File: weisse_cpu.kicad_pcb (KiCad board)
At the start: 2 copper layers, 310 x 260 mm, 22 parts

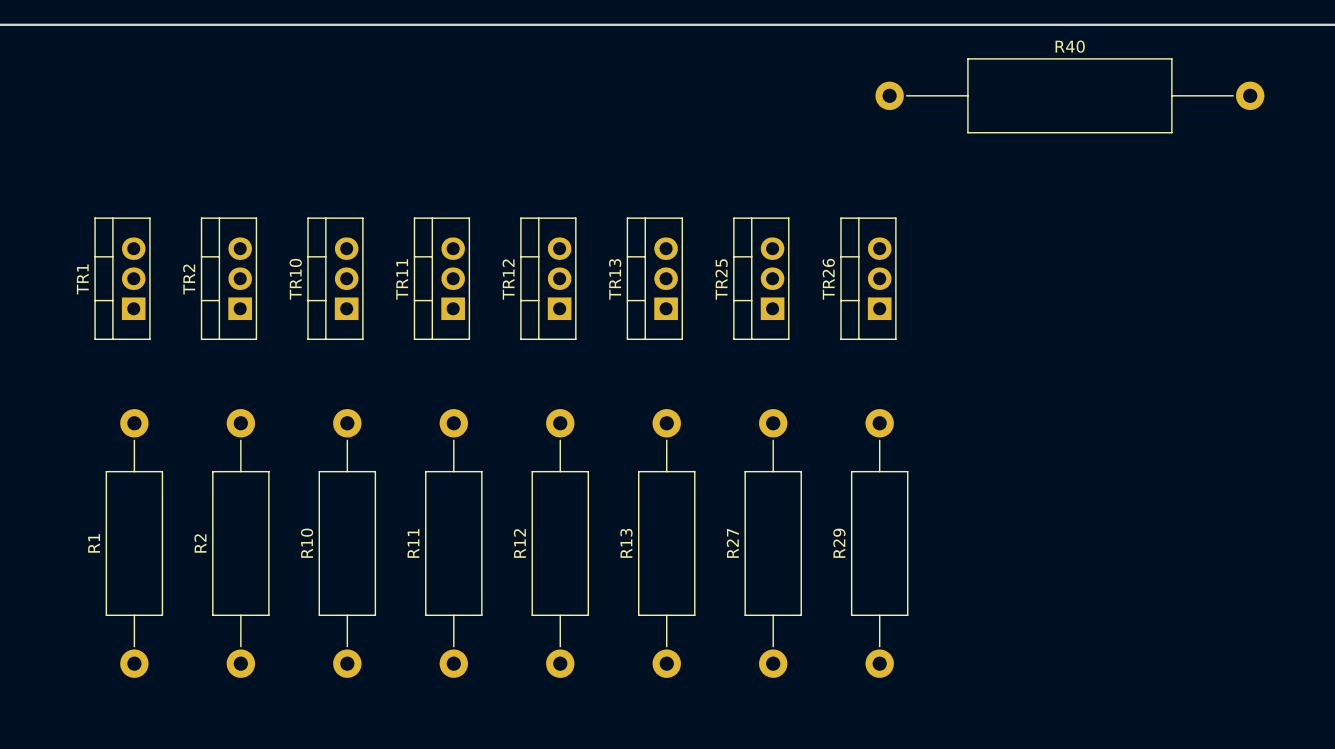
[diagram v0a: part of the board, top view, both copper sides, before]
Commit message: add a bunch of traces
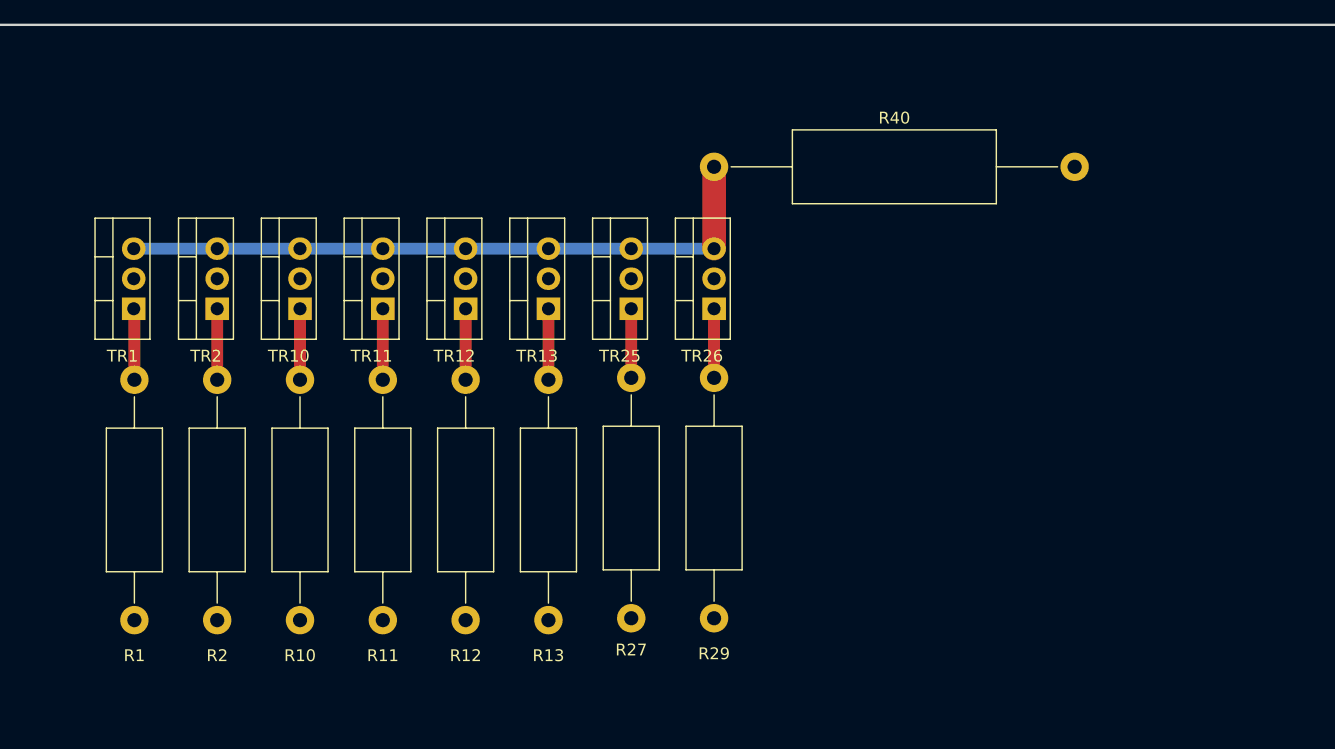
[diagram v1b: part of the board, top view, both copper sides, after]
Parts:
- moved R40 16.0 mm to (216.0, 92.0)
- moved R29 14.5 mm to (216.0, 130.2)
- moved TR26 14.0 mm to (216.0, 104.0)
- moved R27 12.6 mm to (209.0, 130.2)
- moved TR25 11.9 mm to (209.0, 104.0)
- moved R13 10.7 mm to (202.0, 130.3)
- moved TR13 9.94 mm to (202.0, 104.0)
- moved R12 8.81 mm to (195.0, 130.3)
- moved TR12 7.94 mm to (195.0, 104.0)
- moved R11 7.04 mm to (188.0, 130.3)
- moved TR11 5.94 mm to (188.0, 104.0)
- moved R10 5.44 mm to (181.0, 130.3)
- moved R2 4.19 mm to (174.0, 130.3)
- moved TR10 3.94 mm to (181.0, 104.0)
- moved R1 3.68 mm to (167.0, 130.3)
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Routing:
- net Net-(R40-Pad1): track 0.00 -> 56.0 mm
- net Net-(R1-Pad2): track 0.00 -> 6.02 mm
- net Net-(R2-Pad2): track 0.00 -> 6.00 mm
- net Net-(R13-Pad2): track 0.00 -> 6.00 mm
- net Net-(R12-Pad2): track 0.00 -> 6.00 mm
- net Net-(R11-Pad2): track 0.00 -> 6.00 mm
- net Net-(R10-Pad2): track 0.00 -> 6.00 mm
- net Net-(R29-Pad2): track 0.00 -> 5.84 mm
- net Net-(R27-Pad2): track 0.00 -> 5.84 mm

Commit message: serviceabzeige
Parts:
- added ICG10-1: 4066, Package_DIP:DIP-14_W7.62mm, F.Cu at (377.4, 224.8)
- added ICK11: LM324, Package_DIP:DIP-14_W7.62mm, F.Cu at (377.9, 207.6)
- added RM81: R_Pack08, Package_DIP:DIP-16_W7.62mm, F.Cu at (405.1, 224.8)
- added SERVICEANZEIGE+TASTATUR1: Conn_01x20_Male, Connector_PinHeader_2.00mm:PinHeader_1x20_P2.00mm_Vertical, F.Cu at (442.0, 193.0)
- added SIGNALNETZ1: Conn_01x06_Male, Connector_PinHeader_2.00mm:PinHeader_1x06_P2.00mm_Vertical, F.Cu at (442.0, 286.0)
- TR13: value BDX34B -> BDX54C
- moved EINGAENGE1 223.0 mm to (189.0, 88.0)
- moved LEISTUNGSNETZ1 3.61 mm to (442.0, 97.0)
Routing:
- net Net-(LAMPENSPALTEN1-Pad7): track 0.00 -> 2.00 mm
- net Net-(LAMPENSPALTEN1-Pad5): track 0.00 -> 2.00 mm
- net Net-(LAMPENSPALTEN1-Pad3): track 0.00 -> 2.00 mm
- net Net-(LAMPENSPALTEN1-Pad15): track 0.00 -> 2.00 mm
- net Net-(LAMPENSPALTEN1-Pad13): track 0.00 -> 2.00 mm
- net Net-(LAMPENSPALTEN1-Pad11): track 0.00 -> 2.00 mm
- net Net-(LAMPENSPALTEN1-Pad10): track 0.00 -> 2.00 mm
- net Net-(LAMPENSPALTEN1-Pad1): track 0.00 -> 2.00 mm

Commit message: move transistors down
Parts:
- moved R1 11.8 mm to (167.0, 142.2)
- moved R10 11.8 mm to (181.0, 142.2)
- moved R11 11.8 mm to (188.0, 142.2)
- moved R12 11.8 mm to (195.0, 142.2)
- moved R13 11.8 mm to (202.0, 142.2)
- moved R2 11.8 mm to (174.0, 142.2)
- moved R27 11.8 mm to (209.0, 142.0)
- moved R29 11.8 mm to (216.0, 142.0)
- moved TR1 11.8 mm to (166.9, 115.8)
- moved TR10 11.8 mm to (181.0, 115.8)
- moved TR11 11.8 mm to (188.0, 115.8)
- moved TR12 11.8 mm to (195.0, 115.8)
- moved TR13 11.8 mm to (202.0, 115.8)
- moved TR2 11.8 mm to (174.0, 115.8)
- moved TR25 11.8 mm to (209.0, 115.8)
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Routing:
- added copper zone on F.Cu, net GND
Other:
- outline, holes or cut-outs redrawn

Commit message: move connectors
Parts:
- moved ICH4-1 22.1 mm to (238.3, 188.6)
- moved ICG10-1 18.0 mm to (376.5, 206.8)
- moved ICK11 18.0 mm to (377.0, 189.6)
- moved RM81 18.0 mm to (404.2, 206.8)
- moved SERVICEANZEIGE+TASTATUR1 15.0 mm to (442.0, 178.0)
- moved R40 9.03 mm to (222.8, 98.0)
- moved EINGAENGE1 4.00 mm to (193.0, 88.0)
- moved R1 2.24 mm to (169.0, 143.2)
- moved R10 2.24 mm to (183.0, 143.2)
- moved R11 2.24 mm to (190.0, 143.2)
- moved R12 2.24 mm to (197.0, 143.2)
- moved R13 2.24 mm to (204.0, 143.2)
- moved R2 2.24 mm to (176.0, 143.2)
- moved R27 2.24 mm to (211.0, 143.0)
- moved R29 2.24 mm to (218.0, 143.0)
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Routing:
- net Net-(R40-Pad1): track 56.0 -> 49.1 mm
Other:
- outline, holes or cut-outs redrawn

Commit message: move holes
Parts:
- moved R40 5.00 mm to (222.8, 103.0)
- moved LAMPENSPALTEN1 3.16 mm to (148.0, 120.0)
- moved TR32 2.00 mm to (222.0, 162.5)
- moved R1 1.00 mm to (170.0, 143.2)
- moved R10 1.00 mm to (184.0, 143.2)
- moved R11 1.00 mm to (191.0, 143.2)
- moved R12 1.00 mm to (198.0, 143.2)
- moved R13 1.00 mm to (205.0, 143.2)
- moved R2 1.00 mm to (177.0, 143.2)
- moved R27 1.00 mm to (212.0, 143.0)
- moved R29 1.00 mm to (219.0, 143.0)
- moved TR1 1.00 mm to (169.9, 116.8)
- moved TR10 1.00 mm to (184.0, 116.8)
- moved TR11 1.00 mm to (191.0, 116.8)
- moved TR12 1.00 mm to (198.0, 116.8)
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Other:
- outline, holes or cut-outs redrawn

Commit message: add eeprom
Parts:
- added ICC6: 628128_DIP32_SSOP32, Package_DIP:DIP-24_W15.24mm, F.Cu at (300.1, 271.0)
- added ICD6: 27128, Package_DIP:DIP-28_W15.24mm, F.Cu at (295.0, 251.0)
- added ICE6: 27128, Package_DIP:DIP-28_W15.24mm, F.Cu at (295.0, 232.6)
- moved ICG10-1 6.71 mm to (382.5, 203.8)
- moved ICK11 6.71 mm to (383.0, 186.6)
- moved RM81 6.71 mm to (410.2, 203.8)
- moved ICH4-1 3.82 mm to (241.8, 187.0)
- moved R11 3.01 mm to (194.0, 143.4)
- moved R12 3.01 mm to (201.0, 143.4)
- moved R13 3.01 mm to (208.0, 143.4)
- moved R27 3.01 mm to (215.0, 143.2)
- moved R29 3.01 mm to (222.0, 143.2)
- moved TR11 3.01 mm to (194.0, 117.1)
- moved TR12 3.01 mm to (201.0, 117.1)
- moved TR13 3.01 mm to (208.0, 117.1)
- moved TR25 3.01 mm to (215.0, 117.1)
- moved TR26 3.01 mm to (222.0, 117.1)
- moved R10 2.01 mm to (186.0, 143.4)
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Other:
- outline, holes or cut-outs redrawn

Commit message: new photo and new holes
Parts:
- moved ICC6 17.2 mm to (302.6, 288.0)
- moved ICD6 17.2 mm to (297.5, 268.0)
- moved ICE6 17.2 mm to (297.5, 249.6)
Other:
- outline, holes or cut-outs redrawn
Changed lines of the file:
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@@
   )
   (footprint "Package_DIP:DIP-24_W15.24mm" (layer "F.Cu")
-    (at 300.06 271 90)
+    (at 302.56 288 90)
     (descr "24-lead though-hole mounted DIP package, row spacing 15.24 mm (600 mils)")
     (tags "THT DIP DIL PDIP 2.54mm 15.24mm 600mil")
@@
   )
   (footprint "Package_DIP:DIP-28_W15.24mm" (layer "F.Cu")
-    (at 295.015 251.015 90)
+    (at 297.515 268.015 90)
     (descr "28-lead though-hole mounted DIP package, row spacing 15.24 mm (600 mils)")
     (tags "THT DIP DIL PDIP 2.54mm 15.24mm 600mil")
@@
   )
   (footprint "Package_DIP:DIP-28_W15.24mm" (layer "F.Cu")
-    (at 295.015 232.615 90)
+    (at 297.515 249.615 90)
     (descr "28-lead though-hole mounted DIP package, row spacing 15.24 mm (600 mils)")
     (tags "THT DIP DIL PDIP 2.54mm 15.24mm 600mil")
@@
     )
   )
+  (gr_circle (center 350.5 335) (end 353 335)
+    (stroke (width 0.1) (type default)) (fill none) (layer "Edge.Cuts"))
   (gr_line (start 450 340) (end 140 340)
     (stroke (width 0.2) (type solid)) (layer "Edge.Cuts"))
   (gr_line (start 450 80) (end 450 340)
     (stroke (width 0.2) (type solid)) (layer "Edge.Cuts"))
-  (gr_circle (center 232 85) (end 234 85)
+  (gr_circle (center 232 85) (end 234.5 85)
     (stroke (width 0.1) (type default)) (fill none) (layer "Edge.Cuts"))
-  (gr_circle (center 382 85) (end 384 85)
+  (gr_circle (center 381 85) (end 383.5 85)
+    (stroke (width 0.1) (type default)) (fill none) (layer "Edge.Cuts"))
+  (gr_circle (center 201.5 335) (end 204 335)
     (stroke (width 0.1) (type default)) (fill none) (layer "Edge.Cuts"))
   (gr_line (start 140 340) (end 140 80)
     (stroke (width 0.2) (type solid)) (layer "Edge.Cuts"))
+  (gr_circle (center 300 335) (end 301.5 335)
+    (stroke (width 0.1) (type default)) (fill none) (layer "Edge.Cuts"))
   (gr_line (start 140 80) (end 450 80)
     (stroke (width 0.2) (type solid)) (layer "Edge.Cuts"))
-  (gr_circle (center 301 85) (end 302 85)
+  (gr_circle (center 296 85) (end 297.5 85)
     (stroke (width 0.1) (type default)) (fill none) (layer "Edge.Cuts"))
-  (gr_circle (center 281 85) (end 282 85)
+  (gr_circle (center 291 335) (end 292.5 335)
     (stroke (width 0.1) (type default)) (fill none) (layer "Edge.Cuts"))
+  (gr_circle (center 287 85) (end 288.5 85)
+    (stroke (width 0.1) (type default)) (fill none) (layer "Edge.Cuts"))
+  (dimension (type aligned) (layer "Edge.Cuts")
+    (pts (xy 201.5 335) (xy 350.5 335))
+    (height 20.5)
+    (gr_text "149,0000 mm" (at 276 354.35) (layer "Edge.Cuts")
+      (effects (font (size 1 1) (thickness 0.15)))
+    )
+    (format (prefix "") (suffix "") (units 3) (units_format 1) (precision 4))
+    (style (thickness 0.1) (arrow_length 1.27) (text_position_mode 0) (extension_height 0.58642) (extension_offset 0.5) keep_text_aligned)
+  )
+  (dimension (type aligned) (layer "Edge.Cuts")
+    (pts (xy 287 85) (xy 296 85))
+    (height -10)
+    (gr_text "9,0000 mm" (at 291.5 73.85) (layer "Edge.Cuts")
+      (effects (font (size 1 1) (thickness 0.15)))
+    )
+    (format (prefix "") (suffix "") (units 3) (units_format 1) (precision 4))
+    (style (thickness 0.1) (arrow_length 1.27) (text_position_mode 0) (extension_height 0.58642) (extension_offset 0.5) keep_text_aligned)
+  )
+  (dimension (type aligned) (layer "Edge.Cuts")
+    (pts (xy 232 85) (xy 381 85))
+    (height -21)
+    (gr_text "149,0000 mm" (at 306.5 62.85) (layer "Edge.Cuts")
+      (effects (font (size 1 1) (thickness 0.15)))
+    )
+    (format (prefix "") (suffix "") (units 3) (units_format 1) (precision 4))
+    (style (thickness 0.1) (arrow_length 1.27) (text_position_mode 0) (extension_height 0.58642) (extension_offset 0.5) keep_text_aligned)
+  )
+  (dimension (type aligned) (layer "Edge.Cuts")
+    (pts (xy 291 335) (xy 300 335))
+    (height 15)
+    (gr_text "9,0000 mm" (at 295.5 348.85) (layer "Edge.Cuts")
+      (effects (font (size 1 1) (thickness 0.15)))
+    )
+    (format (prefix "") (suffix "") (units 3) (units_format 1) (precision 4))
+    (style (thickness 0.1) (arrow_length 1.27) (text_position_mode 0) (extension_height 0.58642) (extension_offset 0.5) keep_text_aligned)
+  )
+  (dimension (type aligned) (layer "Edge.Cuts")
+    (pts (xy 232 85) (xy 287 85))
+    (height -8)
+    (gr_text "55,0000 mm" (at 259.5 75.85) (layer "Edge.Cuts")
+      (effects (font (size 1 1) (thickness 0.15)))
+    )
+    (format (prefix "") (suffix "") (units 3) (units_format 1) (precision 4))
+    (style (thickness 0.1) (arrow_length 1.27) (text_position_mode 0) (extension_height 0.58642) (extension_offset 0.5) keep_text_aligned)
+  )
+  (dimension (type aligned) (layer "Edge.Cuts")
+    (pts (xy 296 85) (xy 381 85))
+    (height -7)
+    (gr_text "85,0000 mm" (at 338.5 76.85) (layer "Edge.Cuts")
+      (effects (font (size 1 1) (thickness 0.15)))
+    )
+    (format (prefix "") (suffix "") (units 3) (units_format 1) (precision 4))
+    (style (thickness 0.1) (arrow_length 1.27) (text_position_mode 0) (extension_height 0.58642) (extension_offset 0.5) keep_text_aligned)
+  )
   (segment (start 148 118) (end 148 120) (width 1) (layer "F.Cu") (net 135))
   (segment (start 148 114) (end 148 116) (width 1) (layer "F.Cu") (net 136))

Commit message: mirror board
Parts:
- moved ICE6 7.15 mm to (303.0, 245.0)
- moved ICD6 6.02 mm to (303.0, 265.5)
- moved ICC6 5.70 mm to (308.1, 286.5)
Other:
- outline, holes or cut-outs redrawn
- board text added: "ICC6"
- board text added: "ICD6"
- board text added: "ICE6"
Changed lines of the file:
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@@
   )
   (footprint "Package_DIP:DIP-24_W15.24mm" (layer "F.Cu")
-    (at 302.56 288 90)
+    (at 308.06 286.5 90)
     (descr "24-lead though-hole mounted DIP package, row spacing 15.24 mm (600 mils)")
     (tags "THT DIP DIL PDIP 2.54mm 15.24mm 600mil")
@@
   )
   (footprint "Package_DIP:DIP-28_W15.24mm" (layer "F.Cu")
-    (at 297.515 268.015 90)
+    (at 302.98 265.5 90)
     (descr "28-lead though-hole mounted DIP package, row spacing 15.24 mm (600 mils)")
     (tags "THT DIP DIL PDIP 2.54mm 15.24mm 600mil")
@@
   )
   (footprint "Package_DIP:DIP-28_W15.24mm" (layer "F.Cu")
-    (at 297.515 249.615 90)
+    (at 302.98 245 90)
     (descr "28-lead though-hole mounted DIP package, row spacing 15.24 mm (600 mils)")
     (tags "THT DIP DIL PDIP 2.54mm 15.24mm 600mil")
@@
     )
   )
-  (gr_circle (center 350.5 335) (end 353 335)
+  (gr_rect (start 306.5 270) (end 337.5 287.5)
+    (stroke (width 0.15) (type default)) (fill none) (layer "B.SilkS"))
+  (gr_rect (start 301.5 228.5) (end 337.5 246)
+    (stroke (width 0.15) (type default)) (fill none) (layer "B.SilkS"))
+  (gr_rect (start 301.5 249) (end 337.5 266.5)
+    (stroke (width 0.15) (type default)) (fill none) (layer "B.SilkS"))
+  (gr_circle (center 354 335) (end 356.5 335)
     (stroke (width 0.1) (type default)) (fill none) (layer "Edge.Cuts"))
   (gr_line (start 450 340) (end 140 340)
@@
   (gr_line (start 450 80) (end 450 340)
     (stroke (width 0.2) (type solid)) (layer "Edge.Cuts"))
-  (gr_circle (center 232 85) (end 234.5 85)
+  (gr_circle (center 234 85) (end 236.5 85)
     (stroke (width 0.1) (type default)) (fill none) (layer "Edge.Cuts"))
-  (gr_circle (center 381 85) (end 383.5 85)
+  (gr_circle (center 383 85) (end 385.5 85)
     (stroke (width 0.1) (type default)) (fill none) (layer "Edge.Cuts"))
-  (gr_circle (center 201.5 335) (end 204 335)
+  (gr_circle (center 205 335) (end 207.5 335)
     (stroke (width 0.1) (type default)) (fill none) (layer "Edge.Cuts"))
   (gr_line (start 140 340) (end 140 80)
     (stroke (width 0.2) (type solid)) (layer "Edge.Cuts"))
-  (gr_circle (center 300 335) (end 301.5 335)
+  (gr_circle (center 303.5 335) (end 305 335)
     (stroke (width 0.1) (type default)) (fill none) (layer "Edge.Cuts"))
   (gr_line (start 140 80) (end 450 80)
     (stroke (width 0.2) (type solid)) (layer "Edge.Cuts"))
-  (gr_circle (center 296 85) (end 297.5 85)
+  (gr_circle (center 298 85) (end 299.5 85)
     (stroke (width 0.1) (type default)) (fill none) (layer "Edge.Cuts"))
-  (gr_circle (center 291 335) (end 292.5 335)
+  (gr_circle (center 294.5 335) (end 296 335)
     (stroke (width 0.1) (type default)) (fill none) (layer "Edge.Cuts"))
-  (gr_circle (center 287 85) (end 288.5 85)
+  (gr_circle (center 289 85) (end 290.5 85)
     (stroke (width 0.1) (type default)) (fill none) (layer "Edge.Cuts"))
-  (dimension (type aligned) (layer "Edge.Cuts")
-    (pts (xy 201.5 335) (xy 350.5 335))
+  (gr_text "ICD6" (at 312 257.5) (layer "B.SilkS")
+    (effects (font (size 1 1) (thickness 0.15)) (justify mirror))
+  )
+  (gr_text "ICE6" (at 311.5 236) (layer "B.SilkS")
+    (effects (font (size 1 1) (thickness 0.15)) (justify mirror))
+  )
+  (gr_text "ICC6" (at 317 275.5) (layer "B.SilkS")
+    (effects (font (size 1 1) (thickness 0.15)) (justify mirror))
+  )
+  (dimension (type aligned) (layer "User.1")
+    (pts (xy 205 335) (xy 354 335))
     (height 20.5)
-    (gr_text "149,0000 mm" (at 276 354.35) (layer "Edge.Cuts")
+    (gr_text "149,0000 mm" (at 279.5 354.35) (layer "User.1")
       (effects (font (size 1 1) (thickness 0.15)))
     )
@@
     (style (thickness 0.1) (arrow_length 1.27) (text_position_mode 0) (extension_height 0.58642) (extension_offset 0.5) keep_text_aligned)
   )
-  (dimension (type aligned) (layer "Edge.Cuts")
-    (pts (xy 287 85) (xy 296 85))
+  (dimension (type aligned) (layer "User.1")
+    (pts (xy 289 85) (xy 298 85))
     (height -10)
-    (gr_text "9,0000 mm" (at 291.5 73.85) (layer "Edge.Cuts")
+    (gr_text "9,0000 mm" (at 293.5 73.85) (layer "User.1")
       (effects (font (size 1 1) (thickness 0.15)))
     )
@@
     (style (thickness 0.1) (arrow_length 1.27) (text_position_mode 0) (extension_height 0.58642) (extension_offset 0.5) keep_text_aligned)
   )
-  (dimension (type aligned) (layer "Edge.Cuts")
-    (pts (xy 232 85) (xy 381 85))
+  (dimension (type aligned) (layer "User.1")
+    (pts (xy 234 85) (xy 383 85))
     (height -21)
-    (gr_text "149,0000 mm" (at 306.5 62.85) (layer "Edge.Cuts")
+    (gr_text "149,0000 mm" (at 308.5 62.85) (layer "User.1")
       (effects (font (size 1 1) (thickness 0.15)))
     )
@@
     (style (thickness 0.1) (arrow_length 1.27) (text_position_mode 0) (extension_height 0.58642) (extension_offset 0.5) keep_text_aligned)
   )
-  (dimension (type aligned) (layer "Edge.Cuts")
-    (pts (xy 291 335) (xy 300 335))
+  (dimension (type aligned) (layer "User.1")
+    (pts (xy 294.5 335) (xy 303.5 335))
     (height 15)
-    (gr_text "9,0000 mm" (at 295.5 348.85) (layer "Edge.Cuts")
+    (gr_text "9,0000 mm" (at 299 348.85) (layer "User.1")
       (effects (font (size 1 1) (thickness 0.15)))
     )
@@
     (style (thickness 0.1) (arrow_length 1.27) (text_position_mode 0) (extension_height 0.58642) (extension_offset 0.5) keep_text_aligned)
   )
-  (dimension (type aligned) (layer "Edge.Cuts")
-    (pts (xy 232 85) (xy 287 85))
+  (dimension (type aligned) (layer "User.1")
+    (pts (xy 234 85) (xy 289 85))
     (height -8)
-    (gr_text "55,0000 mm" (at 259.5 75.85) (layer "Edge.Cuts")
+    (gr_text "55,0000 mm" (at 261.5 75.85) (layer "User.1")
       (effects (font (size 1 1) (thickness 0.15)))
     )
@@
     (style (thickness 0.1) (arrow_length 1.27) (text_position_mode 0) (extension_height 0.58642) (extension_offset 0.5) keep_text_aligned)
   )
-  (dimension (type aligned) (layer "Edge.Cuts")
-    (pts (xy 296 85) (xy 381 85))
+  (dimension (type aligned) (layer "User.1")
+    (pts (xy 298 85) (xy 383 85))
     (height -7)
-    (gr_text "85,0000 mm" (at 338.5 76.85) (layer "Edge.Cuts")
+    (gr_text "85,0000 mm" (at 340.5 76.85) (layer "User.1")
       (effects (font (size 1 1) (thickness 0.15)))
     )
